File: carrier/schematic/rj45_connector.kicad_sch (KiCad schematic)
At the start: 3 parts, among them J17001 KH-5224-8P8C-D

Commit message: DEF-6: netlist the HDMI-RX TMDS sink termination (new hdmi_rx_term sheet)
The HDMI-RX sink REQUIRES 8x 49.9 ohm/pair-to-AVCC source termination (a
7-series HR bank does not self-terminate TMDS_33) — without it HDMI RX simply
does not work. It had been carried for rounds as a docstring-only MANDATORY
layout note because the resistors belong at the FPGA-bank (receiver) end and
the connector-sheet placer could not anchor an off-sheet AVCC trunk. DEF-6
promotes it to a real, netlisted, gate-checked, BOM-counted network on its own
sheet hdmi_rx_term.py: 8x 49.9R (C114625) from HDMI_RX_{D2,D1,D0,CLK}_{P,N} to
AVCC = +3V3 (bank-33 VCCO IS +3V3, the correct TMDS_33 termination voltage).

LINK PASS (the 3-way TMDS merge with hdmi_rx + som_j2), powertree accepts the
~64 mA termination load, render clean (LAW 1), board PASS 26 sheets,
deterministic, selftest 44/44, m1 PASS.

The 100n/1u AVCC bypass is a documented layout note (not netlisted): the
placer has no pattern for a rail-to-rail cap with no host part on an IC-less
sheet (a tracked placer-robustness follow-up). Inserting the sheet
alphabetically re-stamps the per-sheet reference uniquification of the 15
downstream sheets (U11001->U12001 etc.) — deterministic, a known consequence
of the position-based hierarchy numbering.

Co-Authored-By: Claude Opus 4.8 <noreply@anthropic.com>
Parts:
- renumbered J17001 to J18001, R17001 to R18001, R17002 to R18002
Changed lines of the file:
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@@
 		(property
 			"Reference"
-			"J17001"
+			"J18001"
 			(at 162.56 84.455 0)
 			(effects
@@
 				(path
 					"/c2797150-7a6e-556a-82f5-fdda13c31368/ae92c55a-3f4a-550a-b45e-435ced9eac9f"
-					(reference "J17001")
+					(reference "J18001")
 					(unit 1)
 				)
@@
 		(property
 			"Reference"
-			"R17001"
+			"R18001"
 			(at 133.452 81.28 0)
 			(effects
@@
 				(path
 					"/c2797150-7a6e-556a-82f5-fdda13c31368/ae92c55a-3f4a-550a-b45e-435ced9eac9f"
-					(reference "R17001")
+					(reference "R18001")
 					(unit 1)
 				)
@@
 		(property
 			"Reference"
-			"R17002"
+			"R18002"
 			(at 77.573 81.28 0)
 			(effects
@@
 				(path
 					"/c2797150-7a6e-556a-82f5-fdda13c31368/ae92c55a-3f4a-550a-b45e-435ced9eac9f"
-					(reference "R17002")
+					(reference "R18002")
 					(unit 1)
 				)
@@
 		(property
 			"Reference"
-			"#PWR17001"
+			"#PWR18001"
 			(at 137.16 106.68 0)
 			(effects
@@
 				(path
 					"/c2797150-7a6e-556a-82f5-fdda13c31368/ae92c55a-3f4a-550a-b45e-435ced9eac9f"
-					(reference "#PWR17001")
+					(reference "#PWR18001")
 					(unit 1)
 				)
@@
 		(property
 			"Reference"
-			"#PWR17002"
+			"#PWR18002"
 			(at 130.81 76.2 0)
 			(effects
@@
 				(path
 					"/c2797150-7a6e-556a-82f5-fdda13c31368/ae92c55a-3f4a-550a-b45e-435ced9eac9f"
-					(reference "#PWR17002")
+					(reference "#PWR18002")
 					(unit 1)
 				)
@@
 		(property
 			"Reference"
-			"#PWR17003"
+			"#PWR18003"
 			(at 74.93 76.2 0)
 			(effects
@@
 				(path
 					"/c2797150-7a6e-556a-82f5-fdda13c31368/ae92c55a-3f4a-550a-b45e-435ced9eac9f"
-					(reference "#PWR17003")
+					(reference "#PWR18003")
 					(unit 1)
 				)
@@
 		(property
 			"Reference"
-			"#PWR17004"
+			"#PWR18004"
 			(at 172.72 81.28 0)
 			(effects
@@
 				(path
 					"/c2797150-7a6e-556a-82f5-fdda13c31368/ae92c55a-3f4a-550a-b45e-435ced9eac9f"
-					(reference "#PWR17004")
+					(reference "#PWR18004")
 					(unit 1)
 				)
@@
 		(property
 			"Reference"
-			"#PWR17005"
+			"#PWR18005"
 			(at 172.72 104.14 0)
 			(effects
@@
 				(path
 					"/c2797150-7a6e-556a-82f5-fdda13c31368/ae92c55a-3f4a-550a-b45e-435ced9eac9f"
-					(reference "#PWR17005")
-					(unit 1)
-				)
+					(reference "#PWR18005")
+					(unit 1)
+				)

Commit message: genpolish: TITLE-1 — populate the schematic title block on every sheet
Every sheet rendered a blank Title/Rev/Date — the clearest 'not a real
schematic' tell. emit() now writes a (title_block ...) after the paper node:
title = the sheet circuit's title, company "Zynq SoM Carrier", and a
"<sheet> — generated by schgen (do not hand-edit)" comment. NO date node — a
wall-clock date would break byte-determinism; the content-derived fields keep
every rebuild identical. Verified on A4 (usb_pd) and the dense A3 (power): the
block fills the standard reserved corner with zero drawing overlap. All 26
sheets, goldens re-blessed, board PASS + deterministic, selftest 53/53, m1,
pytest 147.

Co-Authored-By: Claude Opus 4.8 <noreply@anthropic.com>
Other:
- company: (none) -> Zynq SoM Carrier
- title: (none) -> RJ45 8P8C jack (plain, ext. magnetics)
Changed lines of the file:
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@@
 	(generator_version "1.0")
 	(paper "A4")
+	(title_block
+		(title "RJ45 8P8C jack (plain, ext. magnetics)")
+		(company "Zynq SoM Carrier")
+		(comment 1 "rj45_connector — generated by schgen (do not hand-edit)")
+	)
 	(wire
 		(pts

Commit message: board: four board-management HW blocks on a manually-gated +3V3_AUX (BOARDHW)
The four services the carrier was missing — all behind ONE manual power enable
(C1) on two new sheets split so neither defeats the placer's rail-stub router:

  board_aux       — the gate + I2C isolator (infrastructure)
  board_services  — ID-EEPROM + RTC + watchdog + QWIIC (the peripherals)

WHAT LANDED
  * 24AA025E48 (C129895)  ID-EEPROM with a factory EUI-48 **MAC** for the
      LAN8720/RJ45 — strapped 0x51 (0x50 is the FMC EEPROM).
  * RV-3028-C7 (C3019759) I2C RTC, integrated DTCXO (no crystal), CR1220 coin
      cell (KH-CR1220-2) with auto-switchover, 0x52.
  * TPS3823-33 (C7719)    supervisor + windowed watchdog.
  * ZX-SH1.0-4PWT (C7430446)  QWIIC / STEMMA-QT expansion (gated 3V3 + the
      isolated AUX I2C).
  * SY6280 gate + DSHP04 DIP + PCA9306 isolator complete the infrastructure.

CONSTRAINTS (the user's three standing requirements)
  C1 manual enable "like the previous": +3V3_AUX is a SY6280 load switch whose
     EN is a default-OFF DSHP04 DIP (100k pulldown) — the same gated-module
     idiom, self-contained so it touches none of the dense rail/EN sheets.
  C2 "no watchdog reset during power-up": THREE independent guards — (1) the
     supervisor's VDD is the default-OFF +3V3_AUX, so it is UNPOWERED through
     power-up; (2) the TPS3823 disables its watchdog while WDI floats, and WDI
     is driven only by the PL (WATCHDOG_KICK, Hi-Z until the fabric is up); (3)
     RESET# is a firmware-mediated PL EVENT (J3.31), never a rail/POR line.
  C3 Zynq-agnostic: the only SoM-side signals (the 2 watchdog lines) ride PL
     bank-35 IO by their contract net names (IO_L16_N/P_35 -> J3.29/31); xdc.py
     emits the constraints live — nothing hard-codes the Zynq part.

LAW 0 (electrical integrity): the peripherals sit on the GATED rail but their
bus is the always-on STM32_I2C2 management bus. A PCA9306 bridges them with EN
tied to +3V3_AUX, so the switch OPENS whenever the rail is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
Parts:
- renumbered J18001 to J20001, R18001 to R20001, R18002 to R20002
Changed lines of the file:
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@@
 		(property
 			"Reference"
-			"J18001"
+			"J20001"
 			(at 162.56 84.455 0)
 			(effects
@@
 				(path
 					"/c2797150-7a6e-556a-82f5-fdda13c31368/ae92c55a-3f4a-550a-b45e-435ced9eac9f"
-					(reference "J18001")
+					(reference "J20001")
 					(unit 1)
 				)
@@
 		(property
 			"Reference"
-			"R18001"
+			"R20001"
 			(at 133.452 81.28 0)
 			(effects
@@
 				(path
 					"/c2797150-7a6e-556a-82f5-fdda13c31368/ae92c55a-3f4a-550a-b45e-435ced9eac9f"
-					(reference "R18001")
+					(reference "R20001")
 					(unit 1)
 				)
@@
 		(property
 			"Reference"
-			"R18002"
+			"R20002"
 			(at 77.573 81.28 0)
 			(effects
@@
 				(path
 					"/c2797150-7a6e-556a-82f5-fdda13c31368/ae92c55a-3f4a-550a-b45e-435ced9eac9f"
-					(reference "R18002")
+					(reference "R20002")
 					(unit 1)
 				)
@@
 		(property
 			"Reference"
-			"#PWR18001"
+			"#PWR20001"
 			(at 137.16 106.68 0)
 			(effects
@@
 				(path
 					"/c2797150-7a6e-556a-82f5-fdda13c31368/ae92c55a-3f4a-550a-b45e-435ced9eac9f"
-					(reference "#PWR18001")
+					(reference "#PWR20001")
 					(unit 1)
 				)
@@
 		(property
 			"Reference"
-			"#PWR18002"
+			"#PWR20002"
 			(at 130.81 76.2 0)
 			(effects
@@
 				(path
 					"/c2797150-7a6e-556a-82f5-fdda13c31368/ae92c55a-3f4a-550a-b45e-435ced9eac9f"
-					(reference "#PWR18002")
+					(reference "#PWR20002")
 					(unit 1)
 				)
@@
 		(property
 			"Reference"
-			"#PWR18003"
+			"#PWR20003"
 			(at 74.93 76.2 0)
 			(effects
@@
 				(path
 					"/c2797150-7a6e-556a-82f5-fdda13c31368/ae92c55a-3f4a-550a-b45e-435ced9eac9f"
-					(reference "#PWR18003")
+					(reference "#PWR20003")
 					(unit 1)
 				)
@@
 		(property
 			"Reference"
-			"#PWR18004"
+			"#PWR20004"
 			(at 172.72 81.28 0)
 			(effects
@@
 				(path
 					"/c2797150-7a6e-556a-82f5-fdda13c31368/ae92c55a-3f4a-550a-b45e-435ced9eac9f"
-					(reference "#PWR18004")
+					(reference "#PWR20004")
 					(unit 1)
 				)
@@
 		(property
 			"Reference"
-			"#PWR18005"
+			"#PWR20005"
 			(at 172.72 104.14 0)
 			(effects
@@
 				(path
 					"/c2797150-7a6e-556a-82f5-fdda13c31368/ae92c55a-3f4a-550a-b45e-435ced9eac9f"
-					(reference "#PWR18005")
-					(unit 1)
-				)
+					(reference "#PWR20005")
+					(unit 1)
+				)

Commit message: audit fixes: QWIIC ESD on its own sheet + firmware I2C-map completeness
Acting on a multi-agent adversarial re-audit of the 28-sheet board. Each
finding was independently re-verified before action — two confident "HIGH"
findings were FALSE POSITIVES whose proposed fixes would have INTRODUCED bugs,
and are documented-rejected, not applied:

  * "DSHP04 switches in parallel" — wrong. The footprint pads prove the pairing
    by physical opposition (switch n = pads n & 9-n): switch 1 = pads 1&8 is the
    only one on EN_AUX; the other even pins (2/4/6) are NC, identical to the
    proven bringup_rails SW6 idiom. The proposed "fix" (pins 1+2) wires two
    DIFFERENT switches and would leave EN_AUX permanently pulled down — the rail
    could never enable.
  * "PCA9306 EN floats when AUX is off" — wrong. A 100k to a 0 V rail pulls EN
    to 0 V (disabled), which is exactly TI's recommended "isolate when the gated
    side is unpowered" connection. No float.

REAL findings actioned:

1. QWIIC connector lacked ESD (every other external connector has it). Moved the
   QWIIC out of board_services onto its own sheet board_qwiic (the carrier's
   connectors-get-their-own-sheet idiom — rj45_connector, usb_uart_connector)
   and added a USBLC6-2SC6 low-cap ESD array at the connector (1<->6 / 3<->4
   passthrough, clamp ref +3V3_AUX). The dedicated sheet also keeps both sheets
   sparse enough for the rail-stub router. board_services drops to 9 parts.

2. schgen/firmware.py loaded only 7 sheets, so the SC-firmware contract + its
   I2C address-collision check were BLIND to the new devices. Added board_aux/
   board_services to SOURCES and three address rows: FMC-EEPROM 0x50, ID-EEPROM
   0x51 (DERIVED from the 24AA025E48 A1/A0 straps, so a mis-strap to 0x50 now
   trips the collision check against the FMC EEPROM), RTC 0x52. The firmware can
   now address the EUI-48 MAC EEPROM and the RTC. 114 -> 117 #defines.

3. board_services docstring clarified (EEPROM/RTC are on the PCA9306-i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
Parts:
- renumbered J20001 to J21001, R20001 to R21001, R20002 to R21002
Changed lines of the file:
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@@
 		(property
 			"Reference"
-			"J20001"
+			"J21001"
 			(at 162.56 84.455 0)
 			(effects
@@
 				(path
 					"/c2797150-7a6e-556a-82f5-fdda13c31368/ae92c55a-3f4a-550a-b45e-435ced9eac9f"
-					(reference "J20001")
+					(reference "J21001")
 					(unit 1)
 				)
@@
 		(property
 			"Reference"
-			"R20001"
+			"R21001"
 			(at 133.452 81.28 0)
 			(effects
@@
 				(path
 					"/c2797150-7a6e-556a-82f5-fdda13c31368/ae92c55a-3f4a-550a-b45e-435ced9eac9f"
-					(reference "R20001")
+					(reference "R21001")
 					(unit 1)
 				)
@@
 		(property
 			"Reference"
-			"R20002"
+			"R21002"
 			(at 77.573 81.28 0)
 			(effects
@@
 				(path
 					"/c2797150-7a6e-556a-82f5-fdda13c31368/ae92c55a-3f4a-550a-b45e-435ced9eac9f"
-					(reference "R20002")
+					(reference "R21002")
 					(unit 1)
 				)
@@
 		(property
 			"Reference"
-			"#PWR20001"
+			"#PWR21001"
 			(at 137.16 106.68 0)
 			(effects
@@
 				(path
 					"/c2797150-7a6e-556a-82f5-fdda13c31368/ae92c55a-3f4a-550a-b45e-435ced9eac9f"
-					(reference "#PWR20001")
+					(reference "#PWR21001")
 					(unit 1)
 				)
@@
 		(property
 			"Reference"
-			"#PWR20002"
+			"#PWR21002"
 			(at 130.81 76.2 0)
 			(effects
@@
 				(path
 					"/c2797150-7a6e-556a-82f5-fdda13c31368/ae92c55a-3f4a-550a-b45e-435ced9eac9f"
-					(reference "#PWR20002")
+					(reference "#PWR21002")
 					(unit 1)
 				)
@@
 		(property
 			"Reference"
-			"#PWR20003"
+			"#PWR21003"
 			(at 74.93 76.2 0)
 			(effects
@@
 				(path
 					"/c2797150-7a6e-556a-82f5-fdda13c31368/ae92c55a-3f4a-550a-b45e-435ced9eac9f"
-					(reference "#PWR20003")
+					(reference "#PWR21003")
 					(unit 1)
 				)
@@
 		(property
 			"Reference"
-			"#PWR20004"
+			"#PWR21004"
 			(at 172.72 81.28 0)
 			(effects
@@
 				(path
 					"/c2797150-7a6e-556a-82f5-fdda13c31368/ae92c55a-3f4a-550a-b45e-435ced9eac9f"
-					(reference "#PWR20004")
+					(reference "#PWR21004")
 					(unit 1)
 				)
@@
 		(property
 			"Reference"
-			"#PWR20005"
+			"#PWR21005"
 			(at 172.72 104.14 0)
 			(effects
@@
 				(path
 					"/c2797150-7a6e-556a-82f5-fdda13c31368/ae92c55a-3f4a-550a-b45e-435ced9eac9f"
-					(reference "#PWR20005")
-					(unit 1)
-				)
+					(reference "#PWR21005")
+					(unit 1)
+				)

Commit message: buck U1 -> LMR33630 EP buck: power_som split + placer regulator-template generalization
LANDS the exposed-pad buck reselect (the whole point: U1 was a bare TSOT-23-6
TPS54302 with no thermal pad). U1 is now the LMR33630ADDAR (LCSC C841384): TI
SIMPLE SWITCHER, synchronous + internally compensated, 3.8-36 V / 3 A, HSOIC-8
PowerPAD with a REAL datasheet exposed pad, EP (pad 9) netted to GND. Uses the
KiCad STOCK symbol Regulator_Switching:LMR33640ADDA (same DDA pinout, proper
power_in VIN) + the faithful EP-bearing footprint — exactly the TPS54302/
AP2112K stock-symbol idiom. VFB 1.0 V -> 40.2k/10k FB divider = 5.02 V.

SHEET SPLIT (power -> power + power_som): the larger LMR33630 pushed the
4-converter power sheet past one A3 page. The +5V_SOM always-on stage (U4) is
the cleanly-separable unit (only +VIN/+5V_SOM/GND rails cross — they merge by
name; every signal net is internal) and moves to its own subsystem power_som.py.
An auto-paginator cannot split this sheet from the netlist alone (its regulators
chain-share input/output rails, so shared decoupling caps can't be assigned to a
stage); the human split assigns them explicitly. board LINK proves +5V_SOM
merges power_som<->som_j1 and +VIN across pd_input/power/power_mon/power_som.

PLACER GENERALIZATION (schgen/place.py, regulator template) so a richer buck
than the TPS54302's exact 6-pin pinout places — all verified byte-identical for
the 28 unchanged sheets (per-sheet), board gate PASS:
  - _detect_stages: a switch/output pin may be 'output' (LMR SW) not just
    'power_out' (TPS54302 SW); LDO branch stays strict to power_out.
  - _stage_row Edit 1+3: place an aux internal-LDO bias output (LMR VCC, pin 6)
    + its single bypass cap in its own left column (was the "U1_VCC islet, opens
    forbidden" open); emit ALL distinct bottom GND/EP points (not just the last);
    emit explicit NC markers for authored no-connects (the LMR open-collector PG
    pin 4 — was an ERC "Pin not connected").
  - _stage_row Edit 2: ro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
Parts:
- renumbered J21001 to J22001, R21001 to R22001, R21002 to R22002
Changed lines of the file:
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@@
 		(property
 			"Reference"
-			"J21001"
+			"J22001"
 			(at 162.56 84.455 0)
 			(effects
@@
 				(path
 					"/c2797150-7a6e-556a-82f5-fdda13c31368/ae92c55a-3f4a-550a-b45e-435ced9eac9f"
-					(reference "J21001")
+					(reference "J22001")
 					(unit 1)
 				)
@@
 		(property
 			"Reference"
-			"R21001"
+			"R22001"
 			(at 133.452 81.28 0)
 			(effects
@@
 				(path
 					"/c2797150-7a6e-556a-82f5-fdda13c31368/ae92c55a-3f4a-550a-b45e-435ced9eac9f"
-					(reference "R21001")
+					(reference "R22001")
 					(unit 1)
 				)
@@
 		(property
 			"Reference"
-			"R21002"
+			"R22002"
 			(at 77.573 81.28 0)
 			(effects
@@
 				(path
 					"/c2797150-7a6e-556a-82f5-fdda13c31368/ae92c55a-3f4a-550a-b45e-435ced9eac9f"
-					(reference "R21002")
+					(reference "R22002")
 					(unit 1)
 				)
@@
 		(property
 			"Reference"
-			"#PWR21001"
+			"#PWR22001"
 			(at 137.16 106.68 0)
 			(effects
@@
 				(path
 					"/c2797150-7a6e-556a-82f5-fdda13c31368/ae92c55a-3f4a-550a-b45e-435ced9eac9f"
-					(reference "#PWR21001")
+					(reference "#PWR22001")
 					(unit 1)
 				)
@@
 		(property
 			"Reference"
-			"#PWR21002"
+			"#PWR22002"
 			(at 130.81 76.2 0)
 			(effects
@@
 				(path
 					"/c2797150-7a6e-556a-82f5-fdda13c31368/ae92c55a-3f4a-550a-b45e-435ced9eac9f"
-					(reference "#PWR21002")
+					(reference "#PWR22002")
 					(unit 1)
 				)
@@
 		(property
 			"Reference"
-			"#PWR21003"
+			"#PWR22003"
 			(at 74.93 76.2 0)
 			(effects
@@
 				(path
 					"/c2797150-7a6e-556a-82f5-fdda13c31368/ae92c55a-3f4a-550a-b45e-435ced9eac9f"
-					(reference "#PWR21003")
+					(reference "#PWR22003")
 					(unit 1)
 				)
@@
 		(property
 			"Reference"
-			"#PWR21004"
+			"#PWR22004"
 			(at 172.72 81.28 0)
 			(effects
@@
 				(path
 					"/c2797150-7a6e-556a-82f5-fdda13c31368/ae92c55a-3f4a-550a-b45e-435ced9eac9f"
-					(reference "#PWR21004")
+					(reference "#PWR22004")
 					(unit 1)
 				)
@@
 		(property
 			"Reference"
-			"#PWR21005"
+			"#PWR22005"
 			(at 172.72 104.14 0)
 			(effects
@@
 				(path
 					"/c2797150-7a6e-556a-82f5-fdda13c31368/ae92c55a-3f4a-550a-b45e-435ced9eac9f"
-					(reference "#PWR21005")
-					(unit 1)
-				)
+					(reference "#PWR22005")
+					(unit 1)
+				)

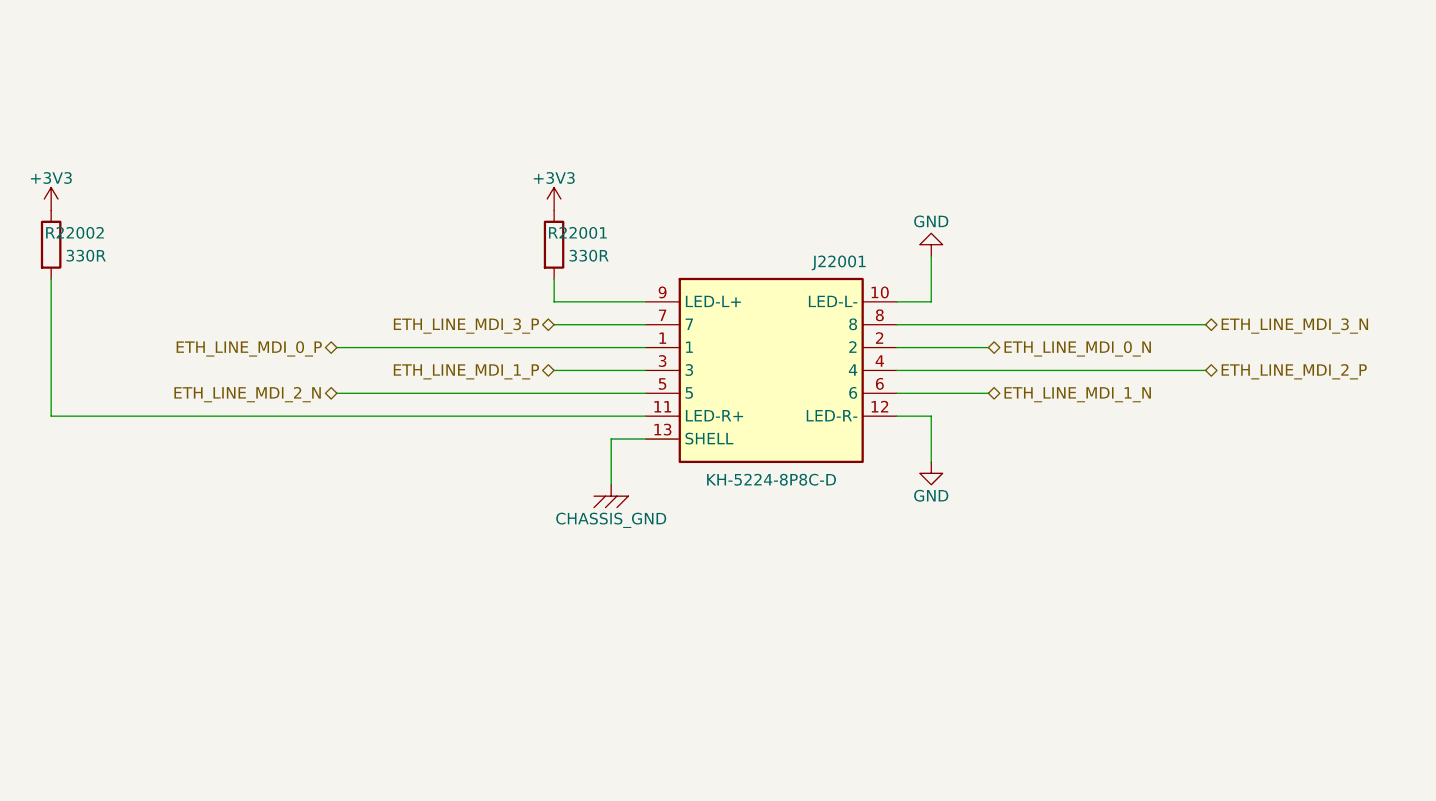
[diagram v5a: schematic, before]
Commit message: carrier: regen artifacts — DEF-H 4x M3 mounting holes + BT1 ML1220 silk '+'
H1-H4 -> CHASSIS_GND on rj45_connector (BOM-excluded plated holes, guard
rejects non-GROUND); BT1 polarity '+' on F.SilkS (LCSC-keyed regen).
Regression green: board (30 sheets), selftest 54/54 + determinism, m1_rc,
pytest 196.

Co-Authored-By: Claude Opus 4.8 <noreply@anthropic.com>
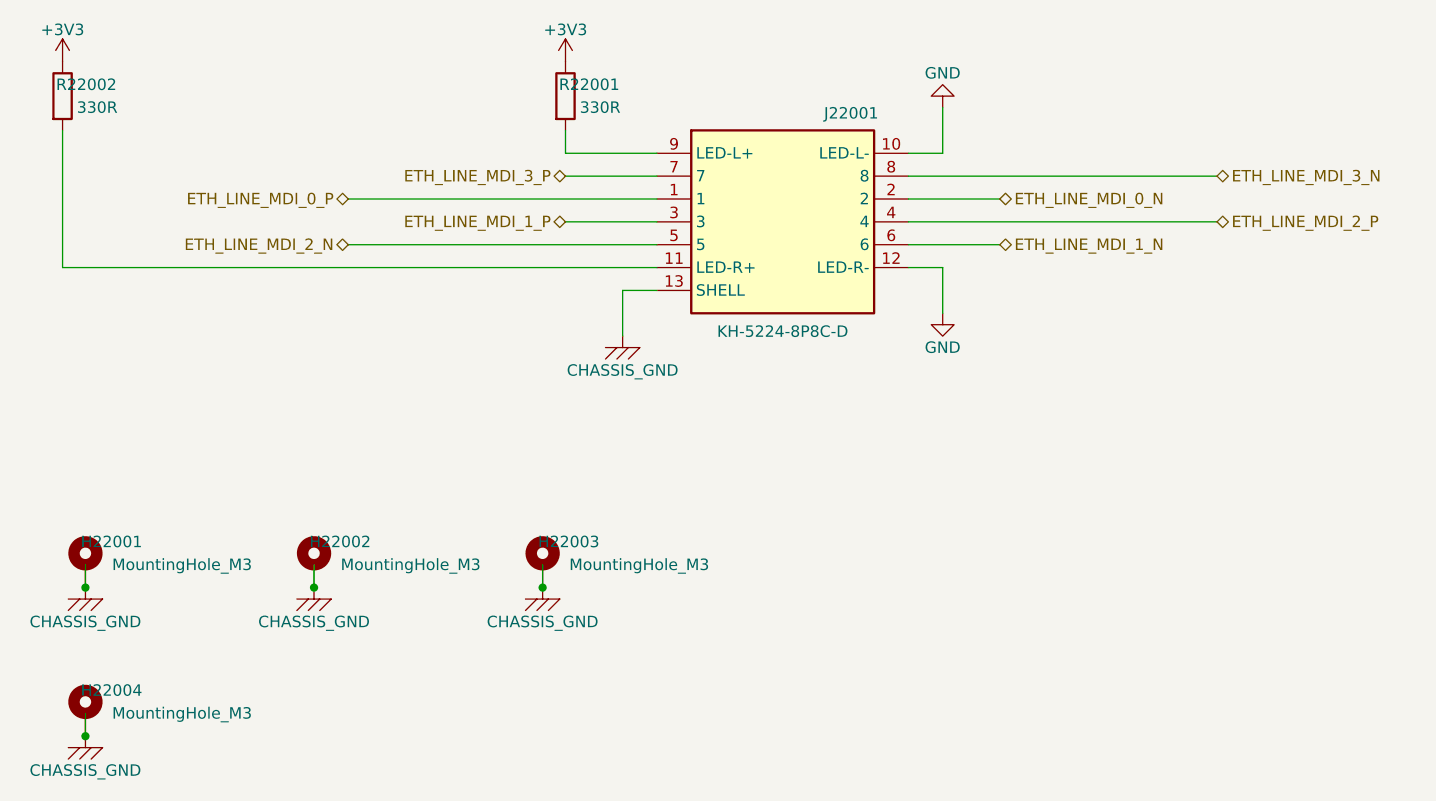
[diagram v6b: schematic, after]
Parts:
- added H22001, H22002, H22003, H22004: MountingHole_M3, MountingHole:MountingHole_3.2mm_M3_Pad, symbol Mechanical:MountingHole_Pad
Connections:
- net CHASSIS_GND: now also H22001.1, H22002.1, H22003.1, H22004.1
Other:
- moved on the sheet: J22001, R22001, R22002
